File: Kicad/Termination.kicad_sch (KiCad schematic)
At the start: 27 parts, among them J1 Conn_02x25_Odd_Even, J5 Conn_02x25_Odd_Even, SW1 219-8MST, U11 DS21S07A, U12 DS21S07A, U8 SN74F244DB

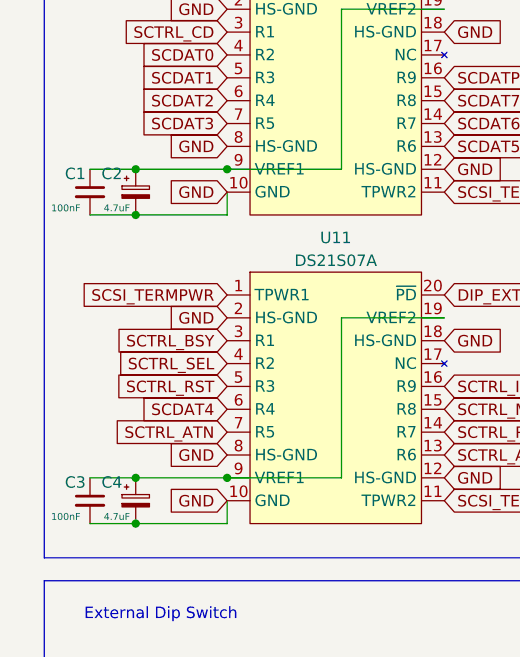
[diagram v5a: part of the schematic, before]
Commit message: Rename capacitors
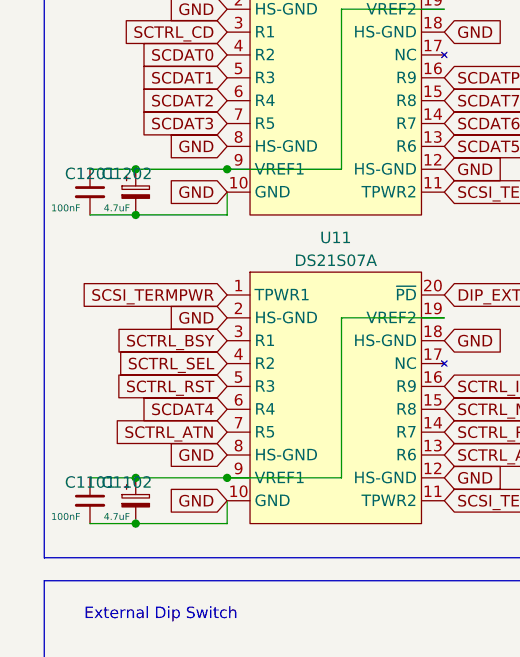
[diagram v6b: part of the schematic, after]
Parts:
- renumbered C3 to C1101, C4 to C1102, C1 to C1201, C2 to C1202
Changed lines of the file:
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@@
 		(on_board yes)
 		(dnp no)
-		(property "Reference" "C3"
+		(property "Reference" "C1101"
 			(at 18.796 80.518 0)
 			(effects
@@
 			(project "A4092"
 				(path "/8f9f4021-47aa-41d9-bea7-f6ccf72098bb/53e9e23b-3b92-4a87-a15c-9c224d6145c5"
-					(reference "C3")
+					(reference "C1101")
 					(unit 1)
 				)
@@
 		(on_board yes)
 		(dnp no)
-		(property "Reference" "C2"
+		(property "Reference" "C1202"
 			(at 22.86 46.228 0)
 			(effects
@@
 			(project ""
 				(path "/8f9f4021-47aa-41d9-bea7-f6ccf72098bb/53e9e23b-3b92-4a87-a15c-9c224d6145c5"
-					(reference "C2")
+					(reference "C1202")
 					(unit 1)
 				)
@@
 		(on_board yes)
 		(dnp no)
-		(property "Reference" "C4"
+		(property "Reference" "C1102"
 			(at 22.86 80.518 0)
 			(effects
@@
 			(project "A4092"
 				(path "/8f9f4021-47aa-41d9-bea7-f6ccf72098bb/53e9e23b-3b92-4a87-a15c-9c224d6145c5"
-					(reference "C4")
+					(reference "C1102")
 					(unit 1)
 				)
@@
 		(on_board yes)
 		(dnp no)
-		(property "Reference" "C1"
+		(property "Reference" "C1201"
 			(at 18.796 46.228 0)
 			(effects
@@
 			(project ""
 				(path "/8f9f4021-47aa-41d9-bea7-f6ccf72098bb/53e9e23b-3b92-4a87-a15c-9c224d6145c5"
-					(reference "C1")
+					(reference "C1201")
 					(unit 1)
 				)

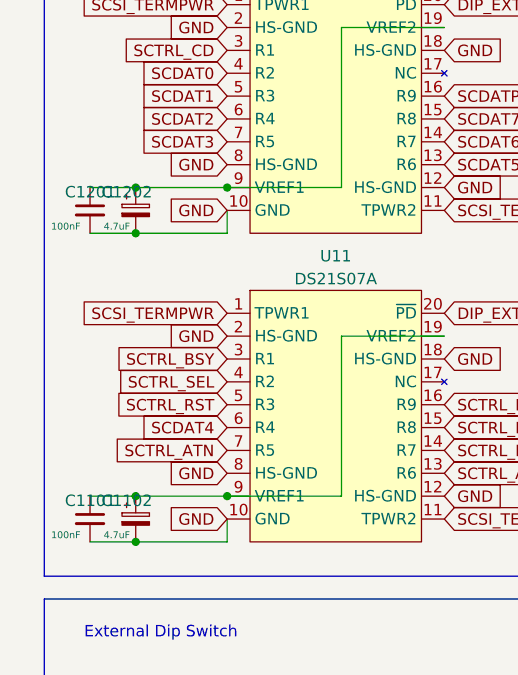
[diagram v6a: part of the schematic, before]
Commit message: Update termination capacitors to tantalum
and clean up bypass caps in schematic
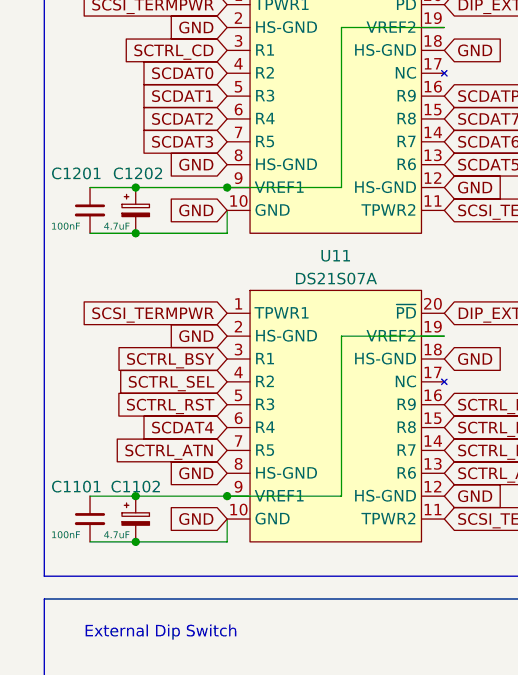
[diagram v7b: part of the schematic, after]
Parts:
- C1102, C1202: footprint Capacitor_SMD:CP_Elec_4x5.7 -> Capacitor_Tantalum_SMD:CP_EIA-3216-10_Kemet-I_HandSolder
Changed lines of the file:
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@@
 		(dnp no)
 		(property "Reference" "C1101"
-			(at 18.796 80.518 0)
+			(at 17.272 78.994 0)
 			(effects
 				(font
@@
 		(dnp no)
 		(property "Reference" "C1202"
-			(at 22.86 46.228 0)
+			(at 24.13 44.196 0)
 			(effects
 				(font
@@
 			)
 		)
-		(property "Footprint" "Capacitor_SMD:CP_Elec_4x5.7"
+		(property "Footprint" "Capacitor_Tantalum_SMD:CP_EIA-3216-10_Kemet-I_HandSolder"
 			(at 26.67 48.26 0)
 			(effects
@@
 		(dnp no)
 		(property "Reference" "C1102"
-			(at 22.86 80.518 0)
+			(at 23.876 78.994 0)
 			(effects
 				(font
@@
 			)
 		)
-		(property "Footprint" "Capacitor_SMD:CP_Elec_4x5.7"
+		(property "Footprint" "Capacitor_Tantalum_SMD:CP_EIA-3216-10_Kemet-I_HandSolder"
 			(at 26.67 82.55 0)
 			(effects
@@
 		(dnp no)
 		(property "Reference" "C1201"
-			(at 18.796 46.228 0)
-			(effects
-				(font
+			(at 17.272 44.196 0)
+			(effects
+				(font

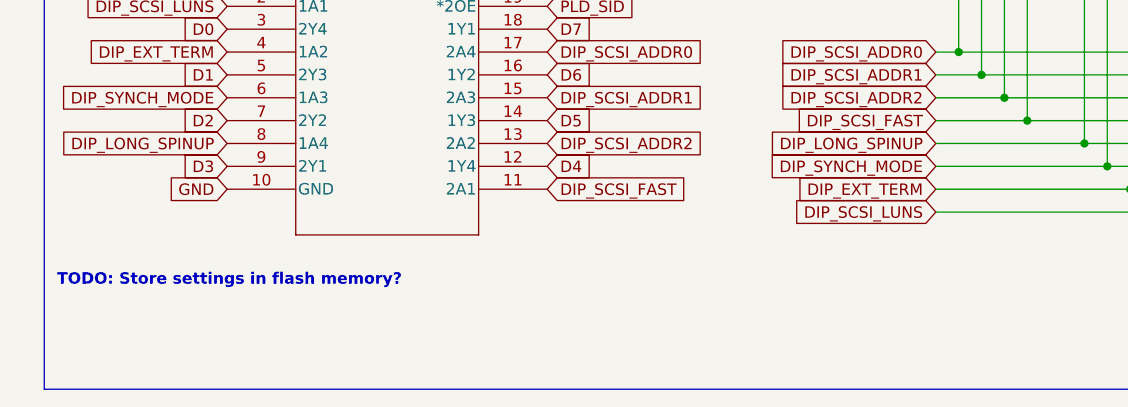
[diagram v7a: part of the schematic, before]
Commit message: Connect DIP_EXT_TERM to CPLD
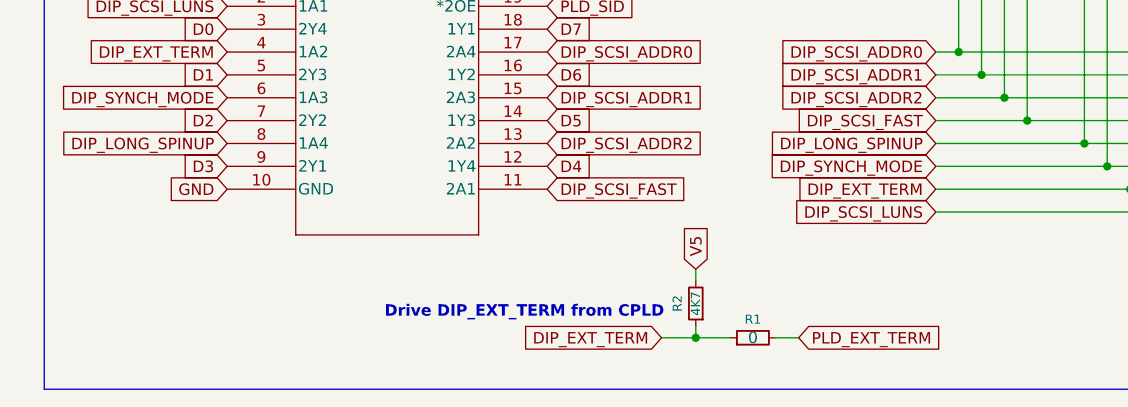
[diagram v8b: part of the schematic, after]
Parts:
- added R1: 0, kicad-official/Resistor_SMD.pretty:R_0603_1608Metric_Pad0.98x0.95mm_HandSolder, symbol Device:R_Small
- added R2: 4K7, kicad-official/Resistor_SMD.pretty:R_0603_1608Metric_Pad0.98x0.95mm_HandSolder, symbol Device:R_Small
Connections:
- net DIP_EXT_TERM: now also R1.1, R2.1
- net V5: now also R2.2
- new net PLD_EXT_TERM: R1.2
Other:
- note added: "Drive DIP_EXT_TERM from CPLD"
- note removed: "TODO: Store settings in flash memory?"
